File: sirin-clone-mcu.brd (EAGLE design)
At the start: 101.6 x 55.9 mm, 21 parts

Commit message: work on lower pcb
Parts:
- removed U$10, U$11, U$12, U$13, U$14, U$15, U$16, U$17, U$3, U$4, U$5, U$6, U$7, U$8, U$9: BOURNS_20K_POTENTIOMETER, sirin-clone-library:BOURNS_PTV09
- removed U$18, U$19, U$20, U$21: ESWITCH__YELLOW, sirin-clone-library:ESWITCH_TL1240YQ1JCLR
- added J1: PJ-002A, sirin-clone-library:CUI_PJ-002A
- U$1: value BOURNS_20K_POTENTIOMETER -> MIDI_CONNECTOR; device sirin-clone-library:BOURNS_PTV09 -> sirin-clone-library:DIN_SDS_50J
- U$2: value BOURNS_20K_POTENTIOMETER -> USB-B; device sirin-clone-library:BOURNS_PTV09 -> sirin-clone-library:USB-B
- moved U$2 79.7 mm to (10.2, 49.5), turned to 180 degrees
- moved U$1 68.8 mm to (33.0, 54.0), turned to 180 degrees
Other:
- board size 101.6 x 55.9 mm -> 101.6 x 57.1 mm

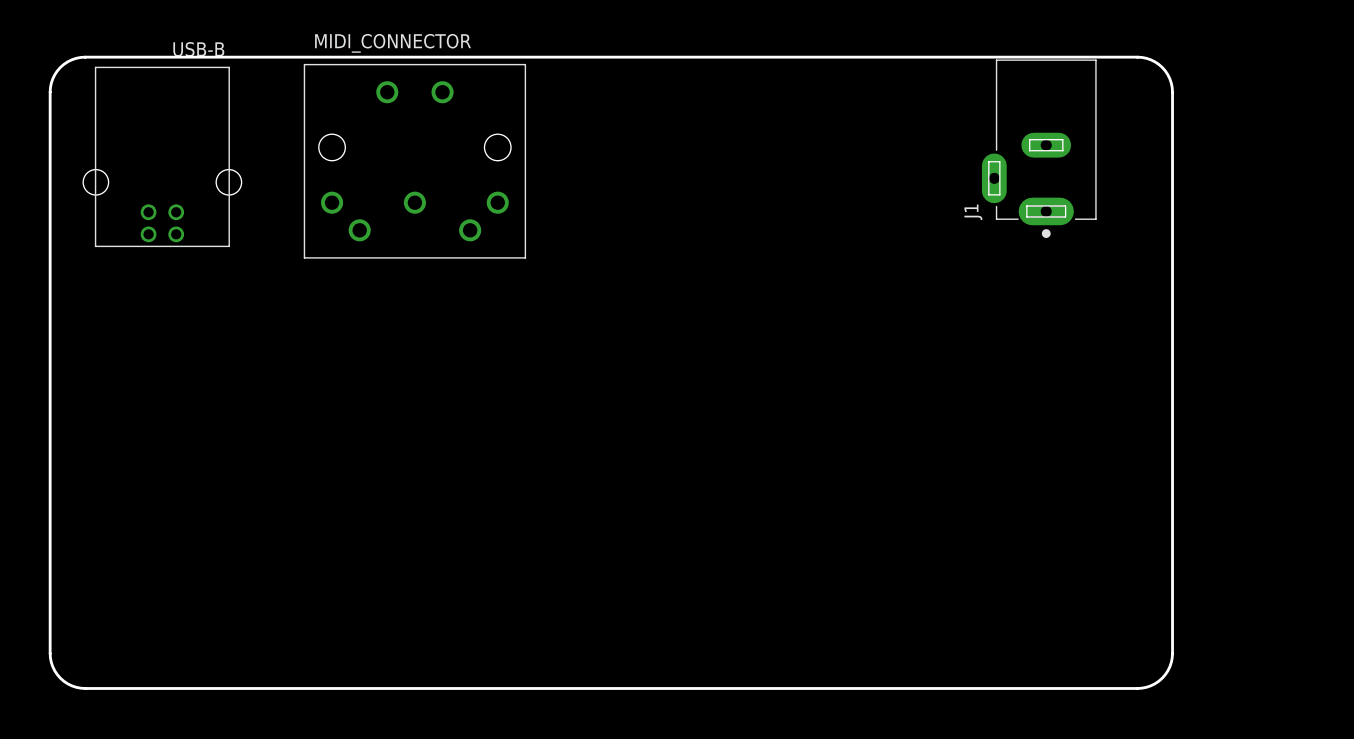
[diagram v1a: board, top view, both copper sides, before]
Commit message: add midi
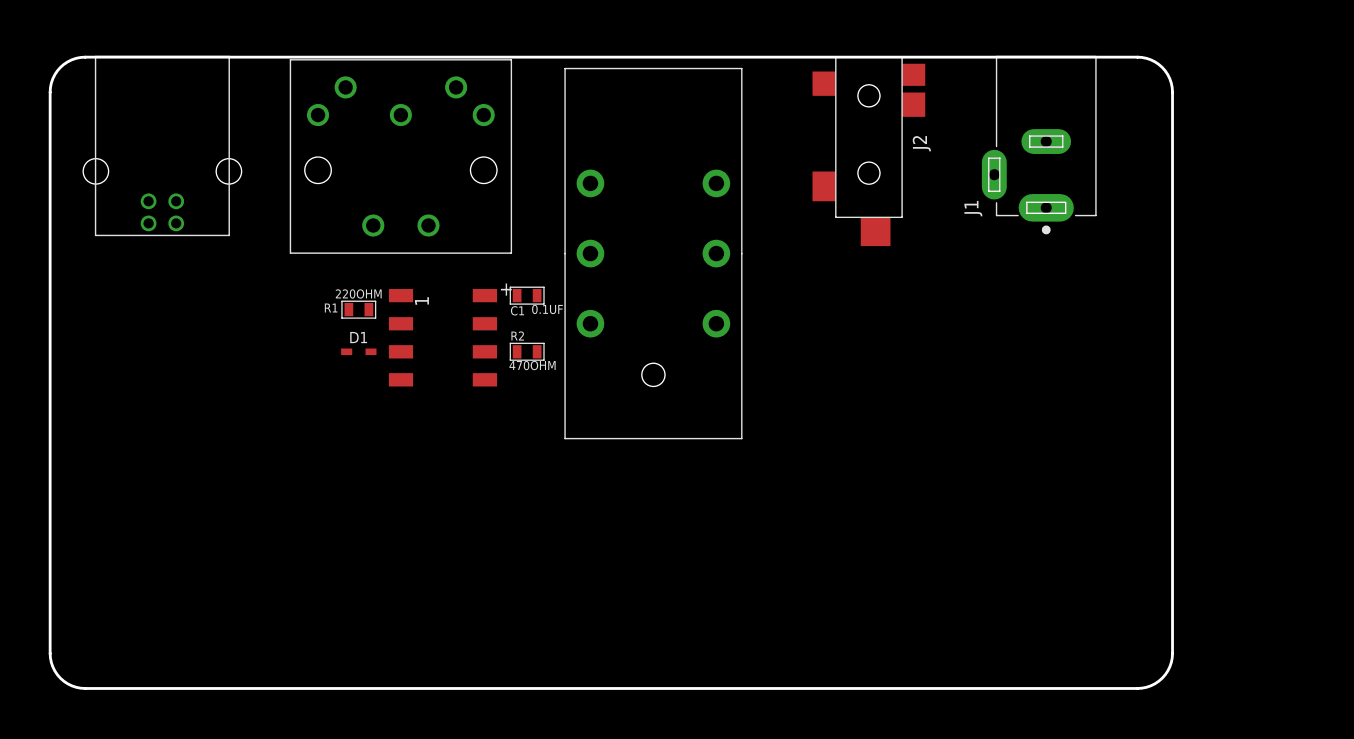
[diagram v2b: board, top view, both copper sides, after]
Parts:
- added C1: 0.1UF, sirin-clone-library:C_0805
- added D1: 1N4148WX-TP, sirin-clone-library:SOD323
- added J2: SWITCHCRAFT_PHONEJACK, sirin-clone-library:STEREO_JACK_2SWITCH
- added OK1: 6N138, sirin-clone-library:DIP8
- added R1: 220OHM, sirin-clone-library:0805
- added R2: 470OHM, sirin-clone-library:0805
- added U$3: STEREO_LINE_OUT_JACK, sirin-clone-library:AMPHENOL_STEREO_JACK
- moved U$1 12.1 mm to (31.8, 41.9), turned to 0 degrees
- moved U$2 0.99 mm to (10.2, 50.5)
- moved J1 0.33 mm to (90.2, 43.5)
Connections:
- new net 3.3V: R2.2
- new net 5V: C1.+, OK1.8
- new net GND: C1.-, OK1.5
- new net N$1: D1.A, OK1.3, U$1.5
- new net N$2: R1.2, U$1.4
- new net N$3: D1.C, OK1.2, R1.1
- new net N$4: OK1.6, R2.1
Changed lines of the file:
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@@
 </layers>
 <board>
-<fusionsync huburn="a.cGVyc29uYWw6dWUyOWViOTli" projecturn="a.cGVyc29uYWw6dWUyOWViOTliIzIwMTkwMjI4MTc5MjYyNDAx" f3durn="urn:adsk.wipprod:dm.lineage:TbYIAYm_SeiHnU5SEeh_ow" pcbguid="427068f0-0b71-4137-912b-b7c28c9918c9" lastpulledtime="2019-03-13T18:23:50Z" lastsyncedchangeguid="93d6f362-9ee9-30fe-d604-cafdce471c4f"/>
+<fusionsync huburn="a.cGVyc29uYWw6dWUyOWViOTli" projecturn="a.cGVyc29uYWw6dWUyOWViOTliIzIwMTkwMjI4MTc5MjYyNDAx" f3durn="urn:adsk.wipprod:dm.lineage:TbYIAYm_SeiHnU5SEeh_ow" pcbguid="427068f0-0b71-4137-912b-b7c28c9918c9" lastpulledtime="2019-03-13T21:24:17Z" lastsyncedchangeguid="ed92bceb-e856-edcd-7f8b-45c6f67b8124"/>
 <plain>
+<wire x1="3.175" y1="0" x2="98.425" y2="0" width="0.254" layer="20"/>
 <wire x1="98.425" y1="0" x2="101.6" y2="3.175" width="0.254" layer="20" curve="90"/>
 <wire x1="101.6" y1="3.175" x2="101.6" y2="53.975" width="0.254" layer="20"/>
@@
 <wire x1="0" y1="53.975" x2="0" y2="3.175" width="0.254" layer="20"/>
 <wire x1="0" y1="3.175" x2="3.175" y2="0" width="0.254" layer="20" curve="90"/>
-<wire x1="3.175" y1="0" x2="98.425" y2="0" width="0.254" layer="20"/>
 </plain>
 <attributes>
@@
 </autorouter>
 <elements>
-<element name="U$1" library="sirin-clone-library" library_urn="urn:adsk.eagle:library:9336050" package="DIN_SDS_50J" package3d_urn="urn:adsk.eagle:package:9699785/3" value="MIDI_CONNECTOR" x="33.02" y="53.975" smashed="yes" rot="R180">
-<attribute name="VALUE" x="38.14" y="59.229" size="1.27" layer="21" rot="R180"/>
-</element>
-<element name="J1" library="sirin-clone-library" library_urn="urn:adsk.eagle:library:9336050" package="CUI_PJ-002A" package3d_urn="urn:adsk.eagle:package:9702177/2" value="PJ-002A" x="90.17" y="43.18" smashed="yes" rot="R90">
-<attribute name="MANUFACTURER" value="CUI INC" x="90.17" y="43.18" size="1.778" layer="27" rot="R90" display="off"/>
-<attribute name="NAME" x="84.034909375" y="42.489428125" size="1.27105" layer="25" rot="R90"/>
-<attribute name="STANDARD" value="Manufacturer recommendations" x="90.17" y="43.18" size="1.778" layer="27" rot="R90" display="off"/>
-<attribute name="VALUE" x="96.587590625" y="42.489184375" size="1.2715" layer="27" rot="R90"/>
-</element>
-<element name="U$2" library="sirin-clone-library" library_urn="urn:adsk.eagle:library:9336050" package="USB-B" package3d_urn="urn:adsk.eagle:package:9702591/4" value="USB-B" x="10.16" y="49.53" smashed="yes" rot="R180">
-<attribute name="VALUE" x="15.875" y="58.493" size="1.27" layer="21" rot="R180"/>
+<element name="J1" library="sirin-clone-library" library_urn="urn:adsk.eagle:library:9336050" package="CUI_PJ-002A" package3d_urn="urn:adsk.eagle:package:9702177/2" value="PJ-002A" x="90.17" y="43.5102" smashed="yes" rot="R90">
+<attribute name="MANUFACTURER" value="CUI INC" x="90.17" y="43.5102" size="1.778" layer="27" rot="R90" display="off"/>
+<attribute name="NAME" x="84.034909375" y="42.819628125" size="1.27105" layer="25" rot="R90"/>
+<attribute name="STANDARD" value="Manufacturer recommendations" x="90.17" y="43.5102" size="1.778" layer="27" rot="R90" display="off"/>
+</element>
+<element name="U$2" library="sirin-clone-library" library_urn="urn:adsk.eagle:library:9336050" package="USB-B" package3d_urn="urn:adsk.eagle:package:9702591/4" value="USB-B" x="10.16" y="50.5206" smashed="yes" rot="R180"/>
+<element name="J2" library="sirin-clone-library" library_urn="urn:adsk.eagle:library:9336050" package="STEREO_JACK_2SWITCH" package3d_urn="urn:adsk.eagle:package:8442329/2" value="SWITCHCRAFT_PHONEJACK" x="71.12" y="57.15" smashed="yes" rot="R270">
+<attribute name="NAME" x="78.105" y="50.165" size="1.27" layer="21" rot="R270"/>
+</element>
+<element name="U$3" library="sirin-clone-library" library_urn="urn:adsk.eagle:library:9336050" package="AMPHENOL_STEREO_JACK" package3d_urn="urn:adsk.eagle:package:9702873/3" value="STEREO_LINE_OUT_JACK" x="54.61" y="39.37" smashed="yes" rot="R90"/>
+<element name="D1" library="sirin-clone-library" library_urn="urn:adsk.eagle:library:9336050" package="SOD323" package3d_urn="urn:adsk.eagle:package:9797239/2" value="1N4148WX-TP" x="27.94" y="30.48" smashed="yes">
+<attribute name="NAME" x="27.04" y="31.26" size="1.016" layer="25"/>
+</element>
+<element name="R1" library="sirin-clone-library" library_urn="urn:adsk.eagle:library:9336050" package="0805" package3d_urn="urn:adsk.eagle:package:8442354/2" value="220OHM" x="27.94" y="34.29" smashed="yes">
+<attribute name="NAME" x="24.765" y="34.036" size="0.8128" layer="21"/>
+<attribute name="VALUE" x="25.781" y="35.306" size="0.8128" layer="21"/>
+</element>
+<element name="C1" library="sirin-clone-library" library_urn="urn:adsk.eagle:library:9336050" package="C_0805" package3d_urn="urn:adsk.eagle:package:8442351/2" value="0.1UF" x="43.18" y="35.56" smashed="yes">
+<attribute name="NAME" x="41.656" y="33.782" size="0.8128" layer="21"/>
+<attribute name="VALUE" x="43.561" y="33.909" size="0.8128" layer="21"/>
+</element>
+<element name="R2" library="sirin-clone-library" library_urn="urn:adsk.eagle:library:9336050" package="0805" package3d_urn="urn:adsk.eagle:package:8442354/2" value="470OHM" x="43.18" y="30.48" smashed="yes">
+<attribute name="NAME" x="41.656" y="31.496" size="0.8128" layer="21"/>
+<attribute name="VALUE" x="41.529" y="28.829" size="0.8128" layer="21"/>
+</element>
+<element name="U$1" library="sirin-clone-library" library_urn="urn:adsk.eagle:library:9336050" package="DIN_SDS_50J" package3d_urn="urn:adsk.eagle:package:9699785/3" value="MIDI_CONNECTOR" x="31.75" y="41.91" smashed="yes"/>
+<element name="OK1" library="sirin-clone-library" library_urn="urn:adsk.eagle:library:9336050" package="DIP8" package3d_urn="urn:adsk.eagle:package:9797260/1" value="6N138" x="35.56" y="31.75" smashed="yes" rot="R270">
+<attribute name="VALUE" x="32.9329" y="24.845" size="1.27" layer="27"/>
 </element>
 </elements>
 <signals>
+<signal name="N$1">
+<contactref element="U$1" pad="5"/>
+<contactref element="OK1" pad="3"/>
+<contactref element="D1" pad="A"/>
+<wire x1="29.04" y1="30.48" x2="26.75" y2="54.41" width="0" layer="19" extent="1-1"/>
+<wire x1="31.76" y1="30.48" x2="29.04" y2="30.48" width="0" layer="19" extent="1-1"/>
+</signal>
+<signal name="N$2">
+<contactref element="R1" pad="2"/>
+<contactref element="U$1" pad="4"/>
+<wire x1="28.84" y1="34.29" x2="36.75" y2="54.41" width="0" layer="19" extent="1-1"/>
+</signal>
+<signal name="N$3">
+<contactref element="R1" pad="1"/>
+<contactref element="OK1" pad="2"/>
+<contactref element="D1" pad="C"/>
+<wire x1="27.04" y1="34.29" x2="31.76" y2="33.02" width="0" layer="19" extent="1-1"/>
+<wire x1="26.84" y1="30.48" x2="27.04" y2="34.29" width="0" layer="19" extent="1-1"/>
+</signal>
+<signal name="5V">
+<contactref element="OK1" pad="8"/>
+<contactref element="C1" pad="+"/>
+<wire x1="42.28" y1="35.56" x2="39.36" y2="35.56" width="0" layer="19" extent="1-1"/>
+</signal>
+<signal name="GND">
+<contactref element="OK1" pad="5"/>
+<contactref element="C1" pad="-"/>
+<wire x1="44.08" y1="35.56" x2="39.36" y2="27.94" width="0" layer="19" extent="1-1"/>
+</signal>
+<signal name="N$4">
+<contactref element="OK1" pad="6"/>
+<contactref element="R2" pad="1"/>
+<wire x1="42.28" y1="30.48" x2="39.36" y2="30.48" width="0" layer="19" extent="1-1"/>
+</signal>
+<signal name="3.3V">
+<contactref element="R2" pad="2"/>
+</signal>
 </signals>
 <mfgpreviewcolors>

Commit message: work on connector options
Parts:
- added J3: 30_PIN_CONNECTOR_MALE, sirin-clone-library:AMPHENOL_30_PIN
- moved U$1 12.8 mm to (32.1, 54.7), turned to 180 degrees
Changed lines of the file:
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@@
 <?xml version="1.0" encoding="utf-8"?>
 <!DOCTYPE eagle SYSTEM "eagle.dtd">
-<eagle version="9.3.0">
+<eagle version="9.3.1">
 <drawing>
 <settings>
@@
 </layers>
 <board>
-<fusionsync huburn="a.cGVyc29uYWw6dWUyOWViOTli" projecturn="a.cGVyc29uYWw6dWUyOWViOTliIzIwMTkwMjI4MTc5MjYyNDAx" f3durn="urn:adsk.wipprod:dm.lineage:TbYIAYm_SeiHnU5SEeh_ow" pcbguid="427068f0-0b71-4137-912b-b7c28c9918c9" lastpulledtime="2019-03-13T21:24:17Z" lastsyncedchangeguid="ed92bceb-e856-edcd-7f8b-45c6f67b8124"/>
+<fusionsync huburn="a.cGVyc29uYWw6dWUyOWViOTli" projecturn="a.cGVyc29uYWw6dWUyOWViOTliIzIwMTkwMjI4MTc5MjYyNDAx" f3durn="urn:adsk.wipprod:dm.lineage:TbYIAYm_SeiHnU5SEeh_ow" pcbguid="427068f0-0b71-4137-912b-b7c28c9918c9" lastpulledtime="2019-03-16T04:38:24Z" lastsyncedchangeguid="db71c5f6-8aba-14b9-3a03-a31893421cc4"/>
 <plain>
+<wire x1="0" y1="3.175" x2="3.175" y2="0" width="0.254" layer="20" curve="90"/>
 <wire x1="3.175" y1="0" x2="98.425" y2="0" width="0.254" layer="20"/>
 <wire x1="98.425" y1="0" x2="101.6" y2="3.175" width="0.254" layer="20" curve="90"/>
@@
 <wire x1="3.175" y1="57.15" x2="0" y2="53.975" width="0.254" layer="20" curve="90"/>
 <wire x1="0" y1="53.975" x2="0" y2="3.175" width="0.254" layer="20"/>
-<wire x1="0" y1="3.175" x2="3.175" y2="0" width="0.254" layer="20" curve="90"/>
 </plain>
 <attributes>
@@
 </autorouter>
 <elements>
-<element name="J1" library="sirin-clone-library" library_urn="urn:adsk.eagle:library:9336050" package="CUI_PJ-002A" package3d_urn="urn:adsk.eagle:package:9702177/2" value="PJ-002A" x="90.17" y="43.5102" smashed="yes" rot="R90">
-<attribute name="MANUFACTURER" value="CUI INC" x="90.17" y="43.5102" size="1.778" layer="27" rot="R90" display="off"/>
-<attribute name="NAME" x="84.034909375" y="42.819628125" size="1.27105" layer="25" rot="R90"/>
-<attribute name="STANDARD" value="Manufacturer recommendations" x="90.17" y="43.5102" size="1.778" layer="27" rot="R90" display="off"/>
-</element>
-<element name="U$2" library="sirin-clone-library" library_urn="urn:adsk.eagle:library:9336050" package="USB-B" package3d_urn="urn:adsk.eagle:package:9702591/4" value="USB-B" x="10.16" y="50.5206" smashed="yes" rot="R180"/>
+<element name="J1" library="sirin-clone-library" library_urn="urn:adsk.eagle:library:9336050" package="CUI_PJ-002A" package3d_urn="urn:adsk.eagle:package:9702177/2" value="PJ-002A" x="90.17" y="43.51" smashed="yes" rot="R90">
+<attribute name="MANUFACTURER" value="CUI INC" x="90.17" y="43.51" size="1.778" layer="27" rot="R90" display="off"/>
+<attribute name="NAME" x="84.034909375" y="42.819428125" size="1.27105" layer="25" rot="R90"/>
+<attribute name="STANDARD" value="Manufacturer recommendations" x="90.17" y="43.51" size="1.778" layer="27" rot="R90" display="off"/>
+</element>
+<element name="U$2" library="sirin-clone-library" library_urn="urn:adsk.eagle:library:9336050" package="USB-B" package3d_urn="urn:adsk.eagle:package:9702591/4" value="USB-B" x="10.16" y="50.521" smashed="yes" rot="R180"/>
 <element name="J2" library="sirin-clone-library" library_urn="urn:adsk.eagle:library:9336050" package="STEREO_JACK_2SWITCH" package3d_urn="urn:adsk.eagle:package:8442329/2" value="SWITCHCRAFT_PHONEJACK" x="71.12" y="57.15" smashed="yes" rot="R270">
 <attribute name="NAME" x="78.105" y="50.165" size="1.27" layer="21" rot="R270"/>
@@
 <attribute name="VALUE" x="41.529" y="28.829" size="0.8128" layer="21"/>
 </element>
-<element name="U$1" library="sirin-clone-library" library_urn="urn:adsk.eagle:library:9336050" package="DIN_SDS_50J" package3d_urn="urn:adsk.eagle:package:9699785/3" value="MIDI_CONNECTOR" x="31.75" y="41.91" smashed="yes"/>
+<element name="U$1" library="sirin-clone-library" library_urn="urn:adsk.eagle:library:9336050" package="DIN_SDS_50J" package3d_urn="urn:adsk.eagle:package:9699785/3" value="MIDI_CONNECTOR" x="32.07" y="54.69" smashed="yes" rot="R180"/>
 <element name="OK1" library="sirin-clone-library" library_urn="urn:adsk.eagle:library:9336050" package="DIP8" package3d_urn="urn:adsk.eagle:package:9797260/1" value="6N138" x="35.56" y="31.75" smashed="yes" rot="R270">
 <attribute name="VALUE" x="32.9329" y="24.845" size="1.27" layer="27"/>
+</element>
+<element name="J3" library="sirin-clone-library" library_urn="urn:adsk.eagle:library:9336050" package="AMPHENOL_30_PIN" package3d_urn="urn:adsk.eagle:package:9858341/2" value="30_PIN_CONNECTOR_MALE" x="83.82" y="7.62" smashed="yes">
+<attribute name="VALUE" x="69.82" y="2.62" size="1.27" layer="21"/>
 </element>
 </elements>
@@
 <contactref element="OK1" pad="3"/>
 <contactref element="D1" pad="A"/>
-<wire x1="29.04" y1="30.48" x2="26.75" y2="54.41" width="0" layer="19" extent="1-1"/>
+<wire x1="29.04" y1="30.48" x2="37.07" y2="42.19" width="0" layer="19" extent="1-1"/>
 <wire x1="31.76" y1="30.48" x2="29.04" y2="30.48" width="0" layer="19" extent="1-1"/>
 </signal>
@@
 <contactref element="R1" pad="2"/>
 <contactref element="U$1" pad="4"/>
-<wire x1="28.84" y1="34.29" x2="36.75" y2="54.41" width="0" layer="19" extent="1-1"/>
+<wire x1="28.84" y1="34.29" x2="27.07" y2="42.19" width="0" layer="19" extent="1-1"/>
 </signal>
 <signal name="N$3">
